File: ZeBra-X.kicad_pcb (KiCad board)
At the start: 2 copper layers, 125 parts, among them J100 CON-SOCJ-2155, Q100 T2N7002AK,LM, U100 LS1205EVD33, U101 SY8003ADFC, U102 SY8003ADFC, U103 SY8003ADFC, U104 SY8003ADFC, U105 BD3539FVM, U200 XC7Z010-2CLG400I

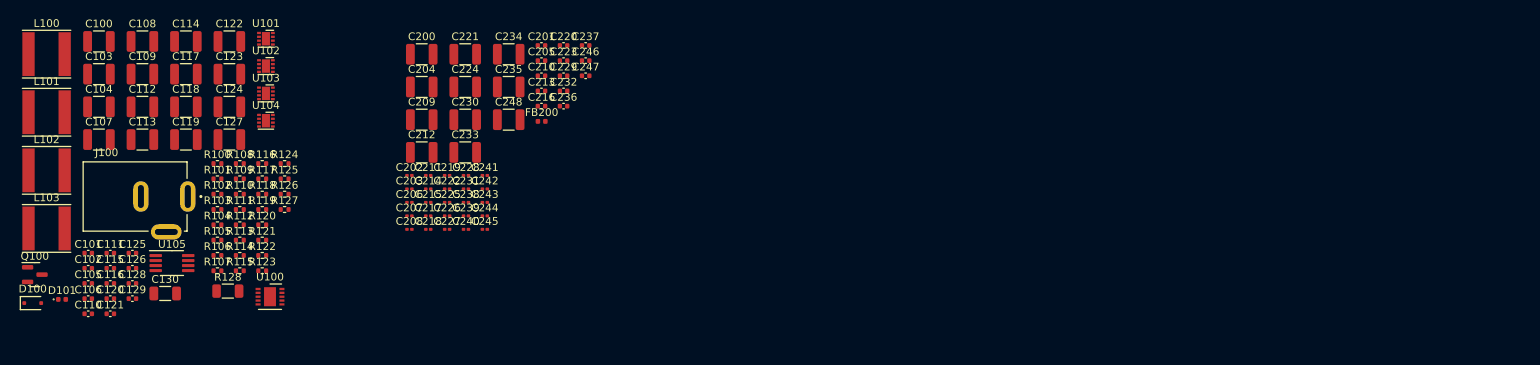
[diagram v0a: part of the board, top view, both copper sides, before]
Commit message: Finished schematic page 4: Zynq Processing System (PS), includes 128MBit QSPI flash, 33.33 MHz PS Clock, and 4Gbyte EMMC Memory
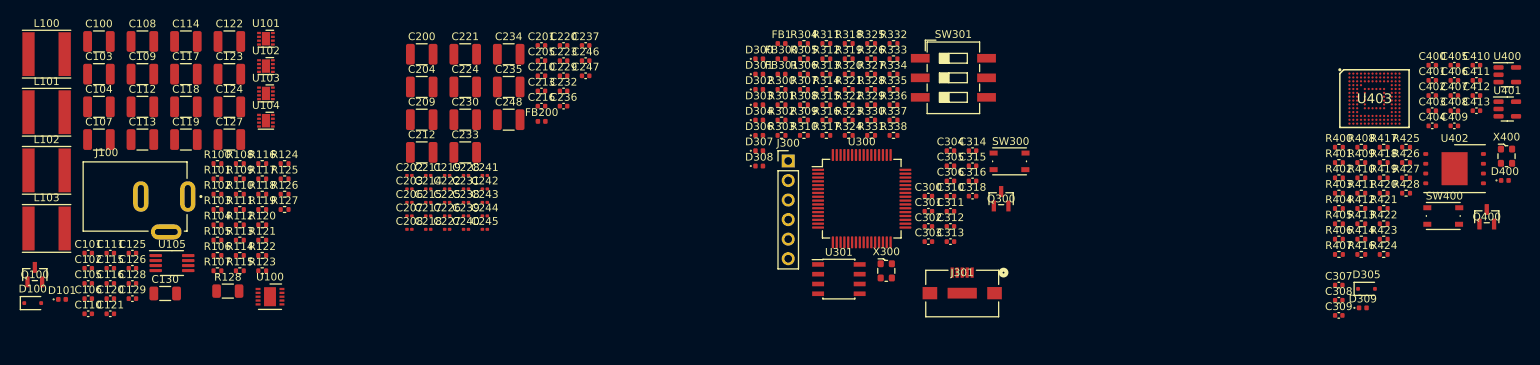
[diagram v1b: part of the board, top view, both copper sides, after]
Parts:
- added C300: 100n, Capacitor_SMD:C_0402_1005Metric, F.Cu at (135.9, 38.3)
- added C301: 4u7, Capacitor_SMD:C_0402_1005Metric, F.Cu at (135.9, 40.2)
- added C302: 4u7, Capacitor_SMD:C_0402_1005Metric, F.Cu at (135.9, 42.2)
- added C303: 4u7, Capacitor_SMD:C_0402_1005Metric, F.Cu at (135.9, 44.2)
- added C304: 100n, Capacitor_SMD:C_0402_1005Metric, F.Cu at (138.7, 32.3)
- added C305: 4u7, Capacitor_SMD:C_0402_1005Metric, F.Cu at (138.7, 34.3)
- added C306: 100n, Capacitor_SMD:C_0402_1005Metric, F.Cu at (138.7, 36.3)
- added C307: 100n, Capacitor_SMD:C_0402_1005Metric, F.Cu at (189.2, 49.8)
- added C308: 100n, Capacitor_SMD:C_0402_1005Metric, F.Cu at (189.2, 51.8)
- added C309: 100n, Capacitor_SMD:C_0402_1005Metric, F.Cu at (189.2, 53.8)
- added C310: 100n, Capacitor_SMD:C_0402_1005Metric, F.Cu at (138.7, 38.3)
- added C311: 100n, Capacitor_SMD:C_0402_1005Metric, F.Cu at (138.7, 40.2)
- added C312: 100n, Capacitor_SMD:C_0402_1005Metric, F.Cu at (138.7, 42.2)
- added C313: 100n, Capacitor_SMD:C_0402_1005Metric, F.Cu at (138.7, 44.2)
- added C314: 100n, Capacitor_SMD:C_0402_1005Metric, F.Cu at (141.6, 32.3)
- added C315: 4u7, Capacitor_SMD:C_0402_1005Metric, F.Cu at (141.6, 34.3)
- added C316: 100n, Capacitor_SMD:C_0402_1005Metric, F.Cu at (141.6, 36.3)
- added C318: 100n, Capacitor_SMD:C_0402_1005Metric, F.Cu at (141.6, 38.3)
- added C400: 100n, Capacitor_SMD:C_0402_1005Metric, F.Cu at (201.3, 21.2)
- added C401: 100n, Capacitor_SMD:C_0402_1005Metric, F.Cu at (201.3, 23.2)
- added C402: 100n, Capacitor_SMD:C_0402_1005Metric, F.Cu at (201.3, 25.2)
- added C403: 100n, Capacitor_SMD:C_0402_1005Metric, F.Cu at (201.3, 27.2)
- added C404: 100n, Capacitor_SMD:C_0402_1005Metric, F.Cu at (201.3, 29.1)
- added C405: 100n, Capacitor_SMD:C_0402_1005Metric, F.Cu at (204.2, 21.2)
- added C406: 100n, Capacitor_SMD:C_0402_1005Metric, F.Cu at (204.2, 23.2)
- added C407: 100n, Capacitor_SMD:C_0402_1005Metric, F.Cu at (204.2, 25.2)
- added C408: 4u7, Capacitor_SMD:C_0402_1005Metric, F.Cu at (204.2, 27.2)
- added C409: 100n, Capacitor_SMD:C_0402_1005Metric, F.Cu at (204.2, 29.1)
- added C410: 4u7, Capacitor_SMD:C_0402_1005Metric, F.Cu at (207.1, 21.2)
- added C411: 4u7, Capacitor_SMD:C_0402_1005Metric, F.Cu at (207.1, 23.2)
- added C412: 100n, Capacitor_SMD:C_0402_1005Metric, F.Cu at (207.1, 25.2)
- added C413: 4u7, Capacitor_SMD:C_0402_1005Metric, F.Cu at (207.1, 27.2)
- added D300: LED_GREEN, LED_SMD:LED_0402_1005Metric, F.Cu at (113.9, 20.4)
- added D301: CG0402MLU-3.3G, Diode_SMD:D_0402_1005Metric, F.Cu at (113.9, 22.4)
- added D302: CG0402MLU-3.3G, Diode_SMD:D_0402_1005Metric, F.Cu at (113.9, 24.4)
- added D303: CG0402MLU-3.3G, Diode_SMD:D_0402_1005Metric, F.Cu at (113.9, 26.4)
- added D304: CG0402MLU-3.3G, Diode_SMD:D_0402_1005Metric, F.Cu at (113.9, 28.4)
- added D305: PMEG1030EJ,115, Diode_SMD:D_SOD-323F, F.Cu at (192.8, 50.3)
- added D306: CG0402MLU-3.3G, Diode_SMD:D_0402_1005Metric, F.Cu at (113.9, 30.4)
- added D307: CG0402MLU-3.3G, Diode_SMD:D_0402_1005Metric, F.Cu at (113.9, 32.4)
- added D308: LED_GREEN, LED_SMD:LED_0402_1005Metric, F.Cu at (113.9, 34.3)
- added D309: LED_GREEN, LED_SMD:LED_0402_1005Metric, F.Cu at (192.3, 52.8)
- added D400: LED_GREEN, LED_SMD:LED_0402_1005Metric, F.Cu at (210.8, 36.2)
- added FB1: 120R, Inductor_SMD:L_0402_1005Metric, F.Cu at (116.8, 18.4)
- added FB300: 120R, Inductor_SMD:L_0402_1005Metric, F.Cu at (116.8, 20.4)
- added FB301: 120R, Inductor_SMD:L_0402_1005Metric, F.Cu at (116.8, 22.4)
- added J300: DigilentH2SHeader, Connector_PinHeader_2.54mm:PinHeader_1x06_P2.54mm_Vertical, F.Cu at (117.7, 33.7)
- added J301: USB3100-30-A, ZeBra_footprints:CONN_USB3100-30-A_GCT, F.Cu at (140.3, 50.9)
- added Q300: T2N7002AK,LM, ZeBra_footprints:SOT23_TOS, F.Cu at (145.3, 38.6)
- added Q400: T2N7002AK,LM, ZeBra_footprints:SOT23_TOS, F.Cu at (208.4, 40.9)
- added R300: 4K7, Resistor_SMD:R_0402_1005Metric, F.Cu at (116.8, 24.4)
- added R301: 4K7, Resistor_SMD:R_0402_1005Metric, F.Cu at (116.8, 26.4)
- added R302: 4K7, Resistor_SMD:R_0402_1005Metric, F.Cu at (116.8, 28.4)
- added R303: 4K7, Resistor_SMD:R_0402_1005Metric, F.Cu at (116.8, 30.4)
- added R304: 4K7, Resistor_SMD:R_0402_1005Metric, F.Cu at (119.7, 18.4)
- added R305: 22R, Resistor_SMD:R_0402_1005Metric, F.Cu at (119.7, 20.4)
- added R306: 22R, Resistor_SMD:R_0402_1005Metric, F.Cu at (119.7, 22.4)
- added R307: 22R, Resistor_SMD:R_0402_1005Metric, F.Cu at (119.7, 24.4)
- added R308: 22R, Resistor_SMD:R_0402_1005Metric, F.Cu at (119.7, 26.4)
- added R309: 510R, Resistor_SMD:R_0402_1005Metric, F.Cu at (119.7, 28.4)
- added R310: 20K, Resistor_SMD:R_0402_1005Metric, F.Cu at (119.7, 30.4)
- added R311: 1K, Resistor_SMD:R_0402_1005Metric, F.Cu at (122.6, 18.4)
- added R312: 20K, Resistor_SMD:R_0402_1005Metric, F.Cu at (122.6, 20.4)
- added R313: 1K, Resistor_SMD:R_0402_1005Metric, F.Cu at (122.6, 22.4)
- added R314: 20K, Resistor_SMD:R_0402_1005Metric, F.Cu at (122.6, 24.4)
- added R315: 1K, Resistor_SMD:R_0402_1005Metric, F.Cu at (122.6, 26.4)
- added R316: 20K, Resistor_SMD:R_0402_1005Metric, F.Cu at (122.6, 28.4)
- added R317: DNP_0R, Resistor_SMD:R_0402_1005Metric, F.Cu at (122.6, 30.4)
- added R318: 1K, Resistor_SMD:R_0402_1005Metric, F.Cu at (125.5, 18.4)
- added R319: 20K, Resistor_SMD:R_0402_1005Metric, F.Cu at (125.5, 20.4)
- added R320: DNP_0R, Resistor_SMD:R_0402_1005Metric, F.Cu at (125.5, 22.4)
- added R321: 1K, Resistor_SMD:R_0402_1005Metric, F.Cu at (125.5, 24.4)
- added R322: 100K, Resistor_SMD:R_0402_1005Metric, F.Cu at (125.5, 26.4)
- added R323: 100K, Resistor_SMD:R_0402_1005Metric, F.Cu at (125.5, 28.4)
- added R324: 12K, Resistor_SMD:R_0402_1005Metric, F.Cu at (125.5, 30.4)
- added R325: 2K49, Resistor_SMD:R_0402_1005Metric, F.Cu at (128.4, 18.4)
- added R326: 12K, Resistor_SMD:R_0402_1005Metric, F.Cu at (128.4, 20.4)
- added R327: 12K, Resistor_SMD:R_0402_1005Metric, F.Cu at (128.4, 22.4)
- added R328: 12K, Resistor_SMD:R_0402_1005Metric, F.Cu at (128.4, 24.4)
- added R329: 22R, Resistor_SMD:R_0402_1005Metric, F.Cu at (128.4, 26.4)
- added R330: 22R, Resistor_SMD:R_0402_1005Metric, F.Cu at (128.4, 28.4)
- added R331: 22R, Resistor_SMD:R_0402_1005Metric, F.Cu at (128.4, 30.4)
- added R332: 22R, Resistor_SMD:R_0402_1005Metric, F.Cu at (131.3, 18.4)
- added R333: 22R, Resistor_SMD:R_0402_1005Metric, F.Cu at (131.3, 20.4)
- added R334: 22R, Resistor_SMD:R_0402_1005Metric, F.Cu at (131.3, 22.4)
- added R335: 22R, Resistor_SMD:R_0402_1005Metric, F.Cu at (131.3, 24.4)
- added R336: 510R, Resistor_SMD:R_0402_1005Metric, F.Cu at (131.3, 26.4)
- added R337: 510R, Resistor_SMD:R_0402_1005Metric, F.Cu at (131.3, 28.4)
- added R338: 22R, Resistor_SMD:R_0402_1005Metric, F.Cu at (131.3, 30.4)
- added R400: 12K, Resistor_SMD:R_0402_1005Metric, F.Cu at (189.2, 31.9)
- added R401: 12K, Resistor_SMD:R_0402_1005Metric, F.Cu at (189.2, 33.9)
- added R402: 12K, Resistor_SMD:R_0402_1005Metric, F.Cu at (189.2, 35.9)
- added R403: 4K7, Resistor_SMD:R_0402_1005Metric, F.Cu at (189.2, 37.9)
- added R404: 20K, Resistor_SMD:R_0402_1005Metric, F.Cu at (189.2, 39.9)
- added R405: 20K, Resistor_SMD:R_0402_1005Metric, F.Cu at (189.2, 41.9)
- added R406: 22R, Resistor_SMD:R_0402_1005Metric, F.Cu at (189.2, 43.8)
- added R407: 22R, Resistor_SMD:R_0402_1005Metric, F.Cu at (189.2, 45.8)
- added R408: 22R, Resistor_SMD:R_0402_1005Metric, F.Cu at (192.1, 31.9)
- added R409: 22R, Resistor_SMD:R_0402_1005Metric, F.Cu at (192.1, 33.9)
- added R410: 22R, Resistor_SMD:R_0402_1005Metric, F.Cu at (192.1, 35.9)
- added R411: 22R, Resistor_SMD:R_0402_1005Metric, F.Cu at (192.1, 37.9)
- added R412: 510R, Resistor_SMD:R_0402_1005Metric, F.Cu at (192.1, 39.9)
- added R413: 12K, Resistor_SMD:R_0402_1005Metric, F.Cu at (192.1, 41.9)
- added R414: 100K, Resistor_SMD:R_0402_1005Metric, F.Cu at (192.1, 43.8)
- added R416: 100K, Resistor_SMD:R_0402_1005Metric, F.Cu at (192.1, 45.8)
- added R417: 12K, Resistor_SMD:R_0402_1005Metric, F.Cu at (195.0, 31.9)
- added R418: 12K, Resistor_SMD:R_0402_1005Metric, F.Cu at (195.0, 33.9)
- added R419: 22R, Resistor_SMD:R_0402_1005Metric, F.Cu at (195.0, 35.9)
- added R420: 22R, Resistor_SMD:R_0402_1005Metric, F.Cu at (195.0, 37.9)
- added R421: 68K, Resistor_SMD:R_0402_1005Metric, F.Cu at (195.0, 39.9)
- added R422: 68K, Resistor_SMD:R_0402_1005Metric, F.Cu at (195.0, 41.9)
- added R423: 68K, Resistor_SMD:R_0402_1005Metric, F.Cu at (195.0, 43.8)
- added R424: 68K, Resistor_SMD:R_0402_1005Metric, F.Cu at (195.0, 45.8)
- added R425: 12K, Resistor_SMD:R_0402_1005Metric, F.Cu at (197.9, 31.9)
- added R426: 12K, Resistor_SMD:R_0402_1005Metric, F.Cu at (197.9, 33.9)
- added R427: 22R, Resistor_SMD:R_0402_1005Metric, F.Cu at (197.9, 35.9)
- added R428: DNP_0R, Resistor_SMD:R_0402_1005Metric, F.Cu at (197.9, 37.9)
- added SW300: SKRPANE010, Button_Switch_SMD:SW_Push_1P1T_NO_Vertical_Wuerth_434133025816, F.Cu at (146.4, 33.7)
- added SW301: 219-3LPST, Button_Switch_SMD:SW_DIP_SPSTx03_Slide_6.7x9.18mm_W8.61mm_P2.54mm_LowProfile, F.Cu at (139.1, 22.9)
- added SW400: SKRPANE010, Button_Switch_SMD:SW_Push_1P1T_NO_Vertical_Wuerth_434133025816, F.Cu at (202.8, 40.8)
- added U300: FT2232HL, Package_QFP:LQFP-64_10x10mm_P0.5mm, F.Cu at (127.2, 38.6)
- added U301: 93LC65B-I/SN, ZeBra_footprints:SOIC-8_3.9x4.9mm_P1.27mm, F.Cu at (124.2, 49.0)
- added U400: 74LVC1G07, Package_TO_SOT_SMD:SOT-23-5, F.Cu at (211.1, 22.5)
- added U401: 74LVC1G07, Package_TO_SOT_SMD:SOT-23-5, F.Cu at (211.1, 26.9)
- added U402: W25Q128JVEIQ, Package_SON:WSON-8-1EP_8x6mm_P1.27mm_EP3.4x4.3mm, F.Cu at (204.2, 34.7)
- added U403: S40FC004C1B2C00000, ZeBra_footprints:BGA153C50P14X14_900X750X80, F.Cu at (193.8, 25.6)
- added X300: ECS-2520MV-120-BN, Oscillator:Oscillator_SMD_ECS_2520MV-xxx-xx-4Pin_2.5x2.0mm, F.Cu at (130.4, 48.0)
- added X400: ECS-2520MV-333.3-BN-TR, Oscillator:Oscillator_SMD_ECS_2520MV-xxx-xx-4Pin_2.5x2.0mm, F.Cu at (211.0, 33.1)
- Q100: footprint Package_TO_SOT_SMD:SOT-23 -> ZeBra_footprints:SOT23_TOS
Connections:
- Q100 pad 1: /[1] Power/LED_PWR_K -> Net-(Q100-G)
- Q100 pad 2: Net-(Q100-G) -> GND
- Q100 pad 3: GND -> /[1] Power/LED_PWR_K
- U200 pad A10: (no net) -> USB_DATA5
- U200 pad A11: (no net) -> USB_CLK
- U200 pad A12: (no net) -> USB_DATA2
- U200 pad A14: (no net) -> USB_DATA0
- U200 pad A15: (no net) -> ETH_RXD3
- U200 pad A16: (no net) -> ETH_RXD1
- U200 pad A17: (no net) -> /[4] Zynq Processing System (PS)/ETH_TXD3
- U200 pad A19: (no net) -> /[4] Zynq Processing System (PS)/ETH_TXCLK
- U200 pad A5: (no net) -> /[4] Zynq Processing System (PS)/QSPI_CLK
- U200 pad A6: (no net) -> QSPI_DQ3_M0
- U200 pad A7: (no net) -> /[4] Zynq Processing System (PS)/QSPI_NCS
- U200 pad A9: (no net) -> MIO43
- U200 pad B10: (no net) -> /[4] Zynq Processing System (PS)/PS_NRST
- U200 pad B12: (no net) -> MIO48
- U200 pad B13: (no net) -> MIO50
- U200 pad B14: (no net) -> MIO47
- U200 pad B15: (no net) -> MIO45
- U200 pad B17: (no net) -> ETH_RXCLK
- U200 pad B18: (no net) -> /[4] Zynq Processing System (PS)/ETH_TXD1
- U200 pad B5: (no net) -> UART1_RX
- U200 pad B7: (no net) -> QSPI_DQ2_M2
- U200 pad B8: (no net) -> QSPI_DQ0_M3
- U200 pad B9: (no net) -> MIO51
- U200 pad C10: (no net) -> ETH_MDC
- U200 pad C11: (no net) -> ETH_MDIO
- U200 pad C12: (no net) -> MIO49
- U200 pad C13: (no net) -> USB_DIR
- U200 pad C15: (no net) -> USB_STP
- U200 pad C16: (no net) -> USB_DATA4
- U200 pad C17: (no net) -> /[4] Zynq Processing System (PS)/ETH_NRST
- U200 pad C18: (no net) -> USB_DATA7
- U200 pad C5: (no net) -> /[4] Zynq Processing System (PS)/SD_D2
- U200 pad C6: (no net) -> /[4] Zynq Processing System (PS)/SD_CMD
- U200 pad C7: (no net) -> PS_NPOR
- U200 pad C8: (no net) -> /[4] Zynq Processing System (PS)/SD_D3
- U200 pad D10: (no net) -> /[4] Zynq Processing System (PS)/ETH_TXD2
- U200 pad D11: (no net) -> ETH_RXD0
- U200 pad D13: (no net) -> ETH_RXCTL
- U200 pad D14: (no net) -> USB_NRST
- U200 pad D15: (no net) -> USB_DATA1
- U200 pad D16: (no net) -> MIO46
- U200 pad D5: (no net) -> UART1_TX_VCFG1
- U200 pad D6: (no net) -> QSPI_DQ1_M1
- U200 pad D8: (no net) -> /[4] Zynq Processing System (PS)/VCFG0
- U200 pad D9: (no net) -> /[4] Zynq Processing System (PS)/SD_CLK
- U200 pad E11: (no net) -> /[4] Zynq Processing System (PS)/MIO_VREF_0V9
- U200 pad E12: (no net) -> ETH_NINT
- U200 pad E13: (no net) -> USB_DATA6
- U200 pad E14: (no net) -> /[4] Zynq Processing System (PS)/ETH_TXD0
- U200 pad E16: (no net) -> USB_NXT
- U200 pad E6: (no net) -> /[4] Zynq Processing System (PS)/PS_LED
- U200 pad E7: (no net) -> /[4] Zynq Processing System (PS)/PS_CLK_33M333
- U200 pad E8: (no net) -> /[4] Zynq Processing System (PS)/SD_D1
- U200 pad E9: (no net) -> /[4] Zynq Processing System (PS)/SD_D0
- U200 pad F12: (no net) -> USB_DATA3
- U200 pad F13: (no net) -> MIO44
- U200 pad F14: (no net) -> /[4] Zynq Processing System (PS)/ETH_TXCTL
- U200 pad F15: (no net) -> ETH_RXD2
- U200 pad F6: (no net) -> /[3] Config, JTAG, Debug/TDO
- U200 pad F9: (no net) -> /[3] Config, JTAG, Debug/TCK
- U200 pad G6: (no net) -> /[3] Config, JTAG, Debug/TDI
- U200 pad J6: (no net) -> /[3] Config, JTAG, Debug/TMS
- U200 pad K10: (no net) -> GND
- U200 pad K9: (no net) -> GND
- U200 pad L10: (no net) -> GND
- U200 pad L6: (no net) -> /[3] Config, JTAG, Debug/NPROGRAM
- U200 pad L9: (no net) -> GND
- U200 pad M10: (no net) -> GND
- U200 pad M6: (no net) -> +3V3
- U200 pad M9: (no net) -> GND
- U200 pad R10: (no net) -> /[3] Config, JTAG, Debug/NINIT
- U200 pad R11: (no net) -> /[3] Config, JTAG, Debug/DONE

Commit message: Added page '[7] 1GB DDR3L Modules'
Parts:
- added C600: 47n, Capacitor_SMD:C_0201_0603Metric, F.Cu at (225.9, 34.7)
- added C601: 47n, Capacitor_SMD:C_0201_0603Metric, F.Cu at (225.9, 36.4)
- added C602: 47n, Capacitor_SMD:C_0201_0603Metric, F.Cu at (225.9, 38.2)
- added C603: 47n, Capacitor_SMD:C_0201_0603Metric, F.Cu at (225.9, 39.9)
- added C604: 470n, Capacitor_SMD:C_0201_0603Metric, F.Cu at (225.9, 41.7)
- added C605: 470n, Capacitor_SMD:C_0201_0603Metric, F.Cu at (225.9, 43.4)
- added C606: 470n, Capacitor_SMD:C_0201_0603Metric, F.Cu at (225.9, 45.2)
- added C607: 470n, Capacitor_SMD:C_0201_0603Metric, F.Cu at (225.9, 46.9)
- added C608: 4u7, Capacitor_SMD:C_0402_1005Metric, F.Cu at (238.4, 34.8)
- added C609: 4u7, Capacitor_SMD:C_0402_1005Metric, F.Cu at (238.4, 36.8)
- added C610: 4u7, Capacitor_SMD:C_0402_1005Metric, F.Cu at (238.4, 38.7)
- added C611: 4u7, Capacitor_SMD:C_0402_1005Metric, F.Cu at (238.4, 40.7)
- added C612: 47n, Capacitor_SMD:C_0201_0603Metric, F.Cu at (228.4, 34.7)
- added C613: 47n, Capacitor_SMD:C_0201_0603Metric, F.Cu at (228.4, 36.4)
- added C700: 47n, Capacitor_SMD:C_0201_0603Metric, F.Cu at (214.0, 57.1)
- added C701: 47n, Capacitor_SMD:C_0201_0603Metric, F.Cu at (214.0, 58.8)
- added C702: 4u7, Capacitor_SMD:C_0402_1005Metric, F.Cu at (224.1, 57.2)
- added C703: 470n, Capacitor_SMD:C_0201_0603Metric, F.Cu at (214.0, 60.6)
- added C704: 47n, Capacitor_SMD:C_0201_0603Metric, F.Cu at (214.0, 62.3)
- added C705: 47n, Capacitor_SMD:C_0201_0603Metric, F.Cu at (214.0, 64.1)
- added C706: 47n, Capacitor_SMD:C_0201_0603Metric, F.Cu at (216.5, 57.1)
- added C707: 47n, Capacitor_SMD:C_0201_0603Metric, F.Cu at (216.5, 58.8)
- added C708: 47n, Capacitor_SMD:C_0201_0603Metric, F.Cu at (216.5, 60.6)
- added C709: 47n, Capacitor_SMD:C_0201_0603Metric, F.Cu at (216.5, 62.3)
- added C710: 47n, Capacitor_SMD:C_0201_0603Metric, F.Cu at (216.5, 64.1)
- added C711: 47n, Capacitor_SMD:C_0201_0603Metric, F.Cu at (218.9, 57.1)
- added C712: 4u7, Capacitor_SMD:C_0402_1005Metric, F.Cu at (224.1, 59.2)
- added C713: 470n, Capacitor_SMD:C_0201_0603Metric, F.Cu at (218.9, 58.8)
- added C714: 47n, Capacitor_SMD:C_0201_0603Metric, F.Cu at (218.9, 60.6)
- added C715: 47n, Capacitor_SMD:C_0201_0603Metric, F.Cu at (218.9, 62.3)
- added C716: 47n, Capacitor_SMD:C_0201_0603Metric, F.Cu at (218.9, 64.1)
- added C717: 47n, Capacitor_SMD:C_0201_0603Metric, F.Cu at (221.4, 57.1)
- added C718: 47n, Capacitor_SMD:C_0201_0603Metric, F.Cu at (221.4, 58.8)
- added C719: 47n, Capacitor_SMD:C_0201_0603Metric, F.Cu at (221.4, 60.6)
- added C720: 47n, Capacitor_SMD:C_0201_0603Metric, F.Cu at (221.4, 62.3)
- added C721: 47n, Capacitor_SMD:C_0201_0603Metric, F.Cu at (221.4, 64.1)
- added C722: 47n, Capacitor_SMD:C_0201_0603Metric, F.Cu at (213.0, 75.2)
- added C723: 47n, Capacitor_SMD:C_0201_0603Metric, F.Cu at (213.0, 77.0)
- added C724: 4u7, Capacitor_SMD:C_0402_1005Metric, F.Cu at (223.0, 75.3)
- added C725: 470n, Capacitor_SMD:C_0201_0603Metric, F.Cu at (213.0, 78.7)
- added C726: 47n, Capacitor_SMD:C_0201_0603Metric, F.Cu at (213.0, 80.5)
- added C727: 47n, Capacitor_SMD:C_0201_0603Metric, F.Cu at (213.0, 82.2)
- added C728: 47n, Capacitor_SMD:C_0201_0603Metric, F.Cu at (215.4, 75.2)
- added C729: 47n, Capacitor_SMD:C_0201_0603Metric, F.Cu at (215.4, 77.0)
- added C730: 47n, Capacitor_SMD:C_0201_0603Metric, F.Cu at (215.4, 78.7)
- added C731: 47n, Capacitor_SMD:C_0201_0603Metric, F.Cu at (215.4, 80.5)
- added C732: 47n, Capacitor_SMD:C_0201_0603Metric, F.Cu at (215.4, 82.2)
- added C733: 47n, Capacitor_SMD:C_0201_0603Metric, F.Cu at (217.9, 75.2)
- added C734: 4u7, Capacitor_SMD:C_0402_1005Metric, F.Cu at (223.0, 77.3)
- added C735: 470n, Capacitor_SMD:C_0201_0603Metric, F.Cu at (217.9, 77.0)
- added C736: 47n, Capacitor_SMD:C_0201_0603Metric, F.Cu at (217.9, 78.7)
- added C737: 47n, Capacitor_SMD:C_0201_0603Metric, F.Cu at (217.9, 80.5)
- added C738: 47n, Capacitor_SMD:C_0201_0603Metric, F.Cu at (217.9, 82.2)
- added C739: 47n, Capacitor_SMD:C_0201_0603Metric, F.Cu at (220.3, 75.2)
- added C740: 47n, Capacitor_SMD:C_0201_0603Metric, F.Cu at (220.3, 77.0)
- added C741: 47n, Capacitor_SMD:C_0201_0603Metric, F.Cu at (220.3, 78.7)
- added C742: 47n, Capacitor_SMD:C_0201_0603Metric, F.Cu at (220.3, 80.5)
- added C743: 47n, Capacitor_SMD:C_0201_0603Metric, F.Cu at (220.3, 82.2)
- added D500: LED_GREEN, LED_SMD:LED_0402_1005Metric, F.Cu at (253.4, 44.8)
- added Q500: T2N7002AK,LM, ZeBra_footprints:SOT23_TOS, F.Cu at (253.9, 41.4)
- added R500: 1K, Resistor_SMD:R_0402_1005Metric, F.Cu at (250.2, 39.9)
- added R501: 100K, Resistor_SMD:R_0402_1005Metric, F.Cu at (250.2, 41.9)
- added R502: 12K, Resistor_SMD:R_0402_1005Metric, F.Cu at (250.2, 43.9)
- added R503: 510R, Resistor_SMD:R_0402_1005Metric, F.Cu at (250.2, 45.8)
- added R600: 100R, Resistor_SMD:R_0201_0603Metric, F.Cu at (228.4, 38.2)
- added R601: 49R9, Resistor_SMD:R_0201_0603Metric, F.Cu at (228.4, 39.9)
- added R602: 49R9, Resistor_SMD:R_0201_0603Metric, F.Cu at (228.4, 41.7)
- added R603: 49R9, Resistor_SMD:R_0201_0603Metric, F.Cu at (228.4, 43.4)
- added R604: 49R9, Resistor_SMD:R_0201_0603Metric, F.Cu at (228.4, 45.2)
- added R605: 49R9, Resistor_SMD:R_0201_0603Metric, F.Cu at (228.4, 46.9)
- added R606: 49R9, Resistor_SMD:R_0201_0603Metric, F.Cu at (230.8, 34.7)
- added R607: 49R9, Resistor_SMD:R_0201_0603Metric, F.Cu at (230.8, 36.4)
- added R608: 49R9, Resistor_SMD:R_0201_0603Metric, F.Cu at (230.8, 38.2)
- added R609: 49R9, Resistor_SMD:R_0201_0603Metric, F.Cu at (230.8, 39.9)
- added R610: 49R9, Resistor_SMD:R_0201_0603Metric, F.Cu at (230.8, 41.7)
- added R611: 49R9, Resistor_SMD:R_0201_0603Metric, F.Cu at (230.8, 43.4)
- added R612: 49R9, Resistor_SMD:R_0201_0603Metric, F.Cu at (230.8, 45.2)
- added R613: 49R9, Resistor_SMD:R_0201_0603Metric, F.Cu at (230.8, 46.9)
- added R614: 49R9, Resistor_SMD:R_0201_0603Metric, F.Cu at (233.3, 34.7)
- added R615: 49R9, Resistor_SMD:R_0201_0603Metric, F.Cu at (233.3, 36.4)
- added R616: 49R9, Resistor_SMD:R_0201_0603Metric, F.Cu at (233.3, 38.2)
- added R617: 49R9, Resistor_SMD:R_0201_0603Metric, F.Cu at (233.3, 39.9)
- added R618: 49R9, Resistor_SMD:R_0201_0603Metric, F.Cu at (233.3, 41.7)
- added R619: 49R9, Resistor_SMD:R_0201_0603Metric, F.Cu at (233.3, 43.4)
- added R620: 49R9, Resistor_SMD:R_0201_0603Metric, F.Cu at (233.3, 45.2)
- added R621: 49R9, Resistor_SMD:R_0201_0603Metric, F.Cu at (233.3, 46.9)
- added R622: 49R9, Resistor_SMD:R_0201_0603Metric, F.Cu at (235.7, 34.7)
- added R623: 49R9, Resistor_SMD:R_0201_0603Metric, F.Cu at (235.7, 36.4)
- added R624: 49R9, Resistor_SMD:R_0201_0603Metric, F.Cu at (235.7, 38.2)
- added R625: 4K7, Resistor_SMD:R_0402_1005Metric, F.Cu at (238.4, 42.7)
- added R626: 100R, Resistor_SMD:R_0201_0603Metric, F.Cu at (235.7, 39.9)
- added R627: 100R, Resistor_SMD:R_0201_0603Metric, F.Cu at (235.7, 41.7)
- added R700: 240R, Resistor_SMD:R_0402_1005Metric, F.Cu at (248.3, 61.4)
- added R701: 240R, Resistor_SMD:R_0402_1005Metric, F.Cu at (248.3, 63.4)
- added U700: MT41K256M16TW-107 IT:P, ZeBra_footprints:FBGA96_TW_MRN, F.Cu at (234.3, 60.8)
- added U701: MT41K256M16TW-107 IT:P, ZeBra_footprints:FBGA96_TW_MRN, F.Cu at (234.3, 79.0)
- moved U200 26.4 mm to (44.0, 97.1)
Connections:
- U200 pad A1: (no net) -> DDR_DM0
- U200 pad A2: (no net) -> DDR_DQ2
- U200 pad A20: (no net) -> unconnected-(U200B-IO_L2N_T0_AD8N_35-PadA20)
- U200 pad A4: (no net) -> DDR_DQ3
- U200 pad B19: (no net) -> unconnected-(U200B-IO_L2P_T0_AD8P_35-PadB19)
- U200 pad B2: (no net) -> DDR_DQS0_N
- U200 pad B20: (no net) -> unconnected-(U200B-IO_L1N_T0_AD0N_35-PadB20)
- U200 pad B3: (no net) -> DDR_DQ1
- U200 pad B4: (no net) -> DDR_NRST
- U200 pad C1: (no net) -> DDR_DQ6
- U200 pad C2: (no net) -> DDR_DQS0_P
- U200 pad C20: (no net) -> unconnected-(U200B-IO_L1P_T0_AD0P_35-PadC20)
- U200 pad C3: (no net) -> DDR_DQ0
- U200 pad D1: (no net) -> DDR_DQ5
- U200 pad D18: (no net) -> PL_B35_L3_N
- U200 pad D19: (no net) -> unconnected-(U200B-IO_L4P_T0_35-PadD19)
- U200 pad D20: (no net) -> unconnected-(U200B-IO_L4N_T0_35-PadD20)
- U200 pad D3: (no net) -> DDR_DQ4
- U200 pad D4: (no net) -> DDR_A13
- U200 pad E1: (no net) -> DDR_DQ7
- U200 pad E17: (no net) -> PL_B35_L3_P
- U200 pad E18: (no net) -> PL_B35_L5_P
- U200 pad E19: (no net) -> PL_B35_L5_N
- U200 pad E2: (no net) -> DDR_DQ8
- U200 pad E3: (no net) -> DDR_DQ9
- U200 pad E4: (no net) -> DDR_A12
- U200 pad F1: (no net) -> DDR_DM1
- U200 pad F16: (no net) -> PL_B35_L6_P
- U200 pad F17: (no net) -> PL_B35_L6_N
- U200 pad F19: (no net) -> unconnected-(U200B-IO_L15P_T2_DQS_AD12P_35-PadF19)
- U200 pad F2: (no net) -> DDR_DQS1_N
- U200 pad F20: (no net) -> unconnected-(U200B-IO_L15N_T2_DQS_AD12N_35-PadF20)
- U200 pad F4: (no net) -> DDR_A14
- U200 pad F5: (no net) -> DDR_A10
- U200 pad G14: (no net) -> unconnected-(U200B-IO_0_35-PadG14)
- U200 pad G15: (no net) -> unconnected-(U200B-IO_L19N_T3_VREF_35-PadG15)
- U200 pad G17: (no net) -> PL_B35_L16_P
- U200 pad G18: (no net) -> PL_B35_L16_N
- U200 pad G19: (no net) -> unconnected-(U200B-IO_L18P_T2_AD13P_35-PadG19)
- U200 pad G2: (no net) -> DDR_DQS1_P
- U200 pad G20: (no net) -> unconnected-(U200B-IO_L18N_T2_AD13N_35-PadG20)
- U200 pad G3: (no net) -> DDR_DQ10
- U200 pad G4: (no net) -> DDR_A11
- U200 pad G5: (no net) -> /[6] Zynq DDR Interface & Termination/DDR_VRN
- U200 pad H1: (no net) -> DDR_DQ14
- U200 pad H15: (no net) -> unconnected-(U200B-IO_L19P_T3_35-PadH15)
- U200 pad H16: (no net) -> PL_B35_L13_P
- U200 pad H17: (no net) -> PL_B35_L13_N
- U200 pad H18: (no net) -> PL_B35_L14_N
- U200 pad H2: (no net) -> DDR_DQ13
- U200 pad H20: (no net) -> unconnected-(U200B-IO_L17N_T2_AD5N_35-PadH20)
- U200 pad H3: (no net) -> DDR_DQ11
- U200 pad H5: (no net) -> /[6] Zynq DDR Interface & Termination/DDR_VRP
- U200 pad H6: (no net) -> +0V675_REF
- U200 pad J1: (no net) -> DDR_DQ15
- U200 pad J14: (no net) -> PL_B35_L20_N
- U200 pad J15: (no net) -> PL_B35_IO25
- U200 pad J16: (no net) -> PL_B35_L24_P
- U200 pad J18: (no net) -> PL_B35_L14_P
- U200 pad J19: (no net) -> unconnected-(U200B-IO_L10N_T1_AD11N_35-PadJ19)
- U200 pad J20: (no net) -> unconnected-(U200B-IO_L17P_T2_AD5P_35-PadJ20)
- U200 pad J3: (no net) -> DDR_DQ12
- U200 pad J4: (no net) -> DDR_A9
- U200 pad J5: (no net) -> DDR_BA2
- U200 pad K1: (no net) -> DDR_A8
- U200 pad K14: (no net) -> PL_B35_L20_P
- U200 pad K16: (no net) -> unconnected-(U200B-IO_L24P_T3_AD15P_35-PadK16)
- U200 pad K17: (no net) -> PL_CLK_125MHZ
- U200 pad K18: (no net) -> unconnected-(U200B-IO_L12N_T1_MRCC_35-PadK18)
- U200 pad K19: (no net) -> unconnected-(U200B-IO_L10P_T1_AD11P_35-PadK19)
- U200 pad K2: (no net) -> DDR_A1
- U200 pad K3: (no net) -> DDR_A3
- U200 pad K4: (no net) -> DDR_A7
- U200 pad L1: (no net) -> DDR_A5
- U200 pad L14: (no net) -> PL_B35_L22_P
- U200 pad L15: (no net) -> PL_B35_L22_N
- U200 pad L16: (no net) -> unconnected-(U200B-IO_L11P_T1_SRCC_35-PadL16)
- U200 pad L17: (no net) -> PL_B35_L11_N
- U200 pad L19: (no net) -> PL_B35_L9_P
- U200 pad L2: (no net) -> DDR_CK_P
- U200 pad L20: (no net) -> PL_B35_L9_N
- U200 pad L4: (no net) -> DDR_A6
- U200 pad L5: (no net) -> DDR_BA0
- U200 pad M14: (no net) -> PL_B35_L23_P
- U200 pad M15: (no net) -> PL_B35_L23_N
- U200 pad M17: (no net) -> PL_B35_L8_P
- U200 pad M18: (no net) -> PL_B35_L8_N
- U200 pad M19: (no net) -> PL_B35_L7_P
- U200 pad M2: (no net) -> DDR_CK_N
- U200 pad M20: (no net) -> PL_B35_L7_N
- U200 pad M3: (no net) -> DDR_A2
- U200 pad M4: (no net) -> DDR_A4
- U200 pad M5: (no net) -> DDR_NWE
- U200 pad N1: (no net) -> DDR_NCS
- U200 pad N15: (no net) -> unconnected-(U200B-IO_L21P_T3_DQS_AD14P_35-PadN15)
- U200 pad N16: (no net) -> unconnected-(U200B-IO_L21N_T3_DQS_AD14N_35-PadN16)
- U200 pad N17: (no net) -> unconnected-(U200A-IO_L23P_T3_34-PadN17)
- U200 pad N18: (no net) -> unconnected-(U200A-IO_L13P_T2_MRCC_34-PadN18)
- U200 pad N2: (no net) -> DDR_A0
- U200 pad N20: (no net) -> PL_B34_L14_P
- U200 pad N3: (no net) -> DDR_CKE
- U200 pad N5: (no net) -> DDR_ODT
- U200 pad P1: (no net) -> DDR_DQ16
- U200 pad P14: (no net) -> unconnected-(U200A-IO_L6P_T0_34-PadP14)
- U200 pad P15: (no net) -> unconnected-(U200A-IO_L24P_T3_34-PadP15)
- U200 pad P16: (no net) -> unconnected-(U200A-IO_L24N_T3_34-PadP16)
- U200 pad P18: (no net) -> unconnected-(U200A-IO_L23N_T3_34-PadP18)
- U200 pad P19: (no net) -> unconnected-(U200A-IO_L13N_T2_MRCC_34-PadP19)
- U200 pad P20: (no net) -> PL_B34_L14_N
- U200 pad P3: (no net) -> DDR_DQ17
- U200 pad P4: (no net) -> DDR_NRAS
- U200 pad P5: (no net) -> DDR_NCAS
- U200 pad P6: (no net) -> +0V675_REF
- U200 pad R1: (no net) -> DDR_DQ19
- U200 pad R14: (no net) -> unconnected-(U200A-IO_L6N_T0_VREF_34-PadR14)
- U200 pad R16: (no net) -> unconnected-(U200A-IO_L19P_T3_34-PadR16)
- U200 pad R17: (no net) -> unconnected-(U200A-IO_L19N_T3_VREF_34-PadR17)
- U200 pad R19: (no net) -> unconnected-(U200A-IO_0_34-PadR19)
- U200 pad R2: (no net) -> DDR_DQS2_P
- U200 pad R3: (no net) -> DDR_DQ18
- U200 pad R4: (no net) -> DDR_BA1
- U200 pad T1: (no net) -> DDR_DM2
- U200 pad T10: (no net) -> unconnected-(U200A-IO_L1N_T0_34-PadT10)
- U200 pad T11: (no net) -> unconnected-(U200A-IO_L1P_T0_34-PadT11)
- U200 pad T12: (no net) -> /[5] Zynq Programmable Logic (PL)/LED_PL
- U200 pad T14: (no net) -> unconnected-(U200A-IO_L5P_T0_34-PadT14)
- U200 pad T15: (no net) -> unconnected-(U200A-IO_L5N_T0_34-PadT15)
- U200 pad T16: (no net) -> unconnected-(U200A-IO_L9P_T1_DQS_34-PadT16)
- U200 pad T17: (no net) -> unconnected-(U200A-IO_L20P_T3_34-PadT17)
- U200 pad T19: (no net) -> unconnected-(U200A-IO_25_34-PadT19)
- U200 pad T2: (no net) -> DDR_DQS2_N
- U200 pad T20: (no net) -> PL_B34_L15_P
- U200 pad T4: (no net) -> DDR_DQ20
- U200 pad U12: (no net) -> unconnected-(U200A-IO_L2N_T0_34-PadU12)
- U200 pad U13: (no net) -> /[5] Zynq Programmable Logic (PL)/NPUDC
- U200 pad U14: (no net) -> PL_B34_L11_P
- U200 pad U15: (no net) -> PL_B34_L11_N
- U200 pad U17: (no net) -> unconnected-(U200A-IO_L9N_T1_DQS_34-PadU17)
- U200 pad U18: (no net) -> unconnected-(U200A-IO_L12P_T1_MRCC_34-PadU18)
- U200 pad U19: (no net) -> unconnected-(U200A-IO_L12N_T1_MRCC_34-PadU19)
- U200 pad U2: (no net) -> DDR_DQ22
- U200 pad U20: (no net) -> PL_B34_L15_N
- U200 pad U3: (no net) -> DDR_DQ23
- U200 pad U4: (no net) -> DDR_DQ21
- U200 pad V1: (no net) -> DDR_DQ24
- U200 pad V12: (no net) -> PL_B34_L4_P
- U200 pad V13: (no net) -> unconnected-(U200A-IO_L3N_T0_DQS_34-PadV13)
- U200 pad V15: (no net) -> PL_B34_L10_P
- U200 pad V16: (no net) -> PL_B34_L18_P
- U200 pad V17: (no net) -> unconnected-(U200A-IO_L21P_T3_DQS_34-PadV17)
- U200 pad V18: (no net) -> unconnected-(U200A-IO_L21N_T3_DQS_34-PadV18)
- U200 pad V2: (no net) -> DDR_DQ30
- U200 pad V20: (no net) -> PL_B34_L16_P
- U200 pad V3: (no net) -> DDR_DQ31
- U200 pad W1: (no net) -> DDR_DQ26
- U200 pad W13: (no net) -> PL_B34_L4_N
- U200 pad W14: (no net) -> PL_B34_L8_P
- U200 pad W15: (no net) -> PL_B34_L10_N
- U200 pad W16: (no net) -> PL_B34_L18_N
- U200 pad W18: (no net) -> PL_B34_L22_P
- U200 pad W19: (no net) -> PL_B34_L22_N
- U200 pad W20: (no net) -> PL_B34_L16_N
- U200 pad W3: (no net) -> DDR_DQ29
- U200 pad W4: (no net) -> DDR_DQS3_N
- U200 pad W5: (no net) -> DDR_DQS3_P
- U200 pad Y1: (no net) -> DDR_DM3
- U200 pad Y14: (no net) -> PL_B34_L8_N
- U200 pad Y16: (no net) -> PL_B34_L7_P
- U200 pad Y17: (no net) -> PL_B34_L7_N
- U200 pad Y18: (no net) -> PL_B34_L17_P
- U200 pad Y19: (no net) -> PL_B34_L17_N
- U200 pad Y2: (no net) -> DDR_DQ28
- U200 pad Y3: (no net) -> DDR_DQ25
- U200 pad Y4: (no net) -> DDR_DQ27
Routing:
- added copper zone on F.Cu, net GND
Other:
- board outline added: 255.3 x 107.1 mm

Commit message: Completed page 8, Gigabit Ethernet Controller
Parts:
- added C800: 4u7, Capacitor_SMD:C_0402_1005Metric, F.Cu at (155.3, 83.5)
- added C801: 100n, Capacitor_SMD:C_0402_1005Metric, F.Cu at (155.3, 85.5)
- added C802: 100n, Capacitor_SMD:C_0402_1005Metric, F.Cu at (155.3, 87.4)
- added C803: 100n, Capacitor_SMD:C_0402_1005Metric, F.Cu at (155.3, 89.4)
- added C804: 100n, Capacitor_SMD:C_0402_1005Metric, F.Cu at (155.3, 91.4)
- added C805: 100n, Capacitor_SMD:C_0402_1005Metric, F.Cu at (158.1, 83.5)
- added C806: 100n, Capacitor_SMD:C_0402_1005Metric, F.Cu at (158.1, 85.5)
- added C807: 100n, Capacitor_SMD:C_0402_1005Metric, F.Cu at (158.1, 87.4)
- added C808: 100n, Capacitor_SMD:C_0402_1005Metric, F.Cu at (158.1, 89.4)
- added C809: 4u7, Capacitor_SMD:C_0402_1005Metric, F.Cu at (158.1, 91.4)
- added C810: 100n, Capacitor_SMD:C_0402_1005Metric, F.Cu at (161.0, 83.5)
- added C811: 100n, Capacitor_SMD:C_0402_1005Metric, F.Cu at (161.0, 85.5)
- added C812: 4u7, Capacitor_SMD:C_0402_1005Metric, F.Cu at (161.0, 87.4)
- added C813: 100n, Capacitor_SMD:C_0402_1005Metric, F.Cu at (161.0, 89.4)
- added C814: 100n, Capacitor_SMD:C_0402_1005Metric, F.Cu at (161.0, 91.4)
- added C815: 4u7, Capacitor_SMD:C_0402_1005Metric, F.Cu at (163.9, 83.5)
- added C816: 4u7, Capacitor_SMD:C_0402_1005Metric, F.Cu at (163.9, 85.5)
- added C817: 100n, Capacitor_SMD:C_0402_1005Metric, F.Cu at (163.9, 87.4)
- added C818: 100n, Capacitor_SMD:C_0402_1005Metric, F.Cu at (163.9, 89.4)
- added C819: 4u7, Capacitor_SMD:C_0402_1005Metric, F.Cu at (163.9, 91.4)
- added FB302: 120R, Inductor_SMD:L_0402_1005Metric, F.Cu at (135.7, 101.7)
- added FB800: 120R, Inductor_SMD:L_0402_1005Metric, F.Cu at (155.3, 69.6)
- added J800: HR911130A, ZeBra_footprints:HANRUN_HR911130A, F.Cu at (144.0, 80.3)
- added L800: 3u3, Inductor_SMD:L_0603_1608Metric, F.Cu at (147.4, 92.7)
- added R800: 4K7, Resistor_SMD:R_0402_1005Metric, F.Cu at (155.3, 71.6)
- added R801: 4K7, Resistor_SMD:R_0402_1005Metric, F.Cu at (155.3, 73.5)
- added R802: DNP_4K7, Resistor_SMD:R_0402_1005Metric, F.Cu at (155.3, 75.5)
- added R803: 1K, Resistor_SMD:R_0402_1005Metric, F.Cu at (155.3, 77.5)
- added R804: 4K7, Resistor_SMD:R_0402_1005Metric, F.Cu at (155.3, 79.5)
- added R805: 1K, Resistor_SMD:R_0402_1005Metric, F.Cu at (155.3, 81.5)
- added R806: 1K, Resistor_SMD:R_0402_1005Metric, F.Cu at (158.2, 69.6)
- added R807: 22R, Resistor_SMD:R_0402_1005Metric, F.Cu at (158.2, 71.6)
- added R808: 22R, Resistor_SMD:R_0402_1005Metric, F.Cu at (158.2, 73.5)
- added R809: 22R, Resistor_SMD:R_0402_1005Metric, F.Cu at (158.2, 75.5)
- added R810: 22R, Resistor_SMD:R_0402_1005Metric, F.Cu at (158.2, 77.5)
- added R811: 22R, Resistor_SMD:R_0402_1005Metric, F.Cu at (158.2, 79.5)
- added R812: 22R, Resistor_SMD:R_0402_1005Metric, F.Cu at (158.2, 81.5)
- added R813: 1K, Resistor_SMD:R_0402_1005Metric, F.Cu at (161.1, 69.6)
- added R814: 1K, Resistor_SMD:R_0402_1005Metric, F.Cu at (161.1, 71.6)
- added R815: 22R, Resistor_SMD:R_0402_1005Metric, F.Cu at (161.1, 73.5)
- added R816: 22R, Resistor_SMD:R_0402_1005Metric, F.Cu at (161.1, 75.5)
- added R817: 22R, Resistor_SMD:R_0402_1005Metric, F.Cu at (161.1, 77.5)
- added R818: 4K7, Resistor_SMD:R_0402_1005Metric, F.Cu at (161.1, 79.5)
- added R819: 4K7, Resistor_SMD:R_0402_1005Metric, F.Cu at (161.1, 81.5)
- added R820: 4K7, Resistor_SMD:R_0402_1005Metric, F.Cu at (164.0, 69.6)
- added R821: 2K49, Resistor_SMD:R_0402_1005Metric, F.Cu at (164.0, 71.6)
- added R822: 510R, Resistor_SMD:R_0402_1005Metric, F.Cu at (164.0, 73.5)
- added R823: 510R, Resistor_SMD:R_0402_1005Metric, F.Cu at (164.0, 75.5)
- added U800: RTL8211F-CG, Package_DFN_QFN:QFN-40-1EP_5x5mm_P0.4mm_EP3.8x3.8mm, F.Cu at (137.9, 95.1)
- added X800: ECS-2520MV-250-BN-TR, Oscillator:Oscillator_SMD_ECS_2520MV-xxx-xx-4Pin_2.5x2.0mm, F.Cu at (143.5, 93.6)
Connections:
- FB1 pad 1: +3V3 -> +3V3_ETH
- FB1 pad 2: Net-(U300-VPHY) -> +3V3

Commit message: finished page 9, USB 2.0 Hub
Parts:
- added C900: 100n, Capacitor_SMD:C_0402_1005Metric, F.Cu at (190.1, 93.7)
- added C901: 100n, Capacitor_SMD:C_0402_1005Metric, F.Cu at (190.1, 95.6)
- added C902: 100n, Capacitor_SMD:C_0402_1005Metric, F.Cu at (190.1, 97.6)
- added C903: 100n, Capacitor_SMD:C_0402_1005Metric, F.Cu at (190.1, 99.6)
- added C904: 100n, Capacitor_SMD:C_0402_1005Metric, F.Cu at (190.1, 101.6)
- added C905: 4u7, Capacitor_SMD:C_0402_1005Metric, F.Cu at (190.1, 103.5)
- added C906: 4u7, Capacitor_SMD:C_0402_1005Metric, F.Cu at (190.1, 105.5)
- added C907: 4u7, Capacitor_SMD:C_0402_1005Metric, F.Cu at (217.0, 108.1)
- added C908: 4u7, Capacitor_SMD:C_0402_1005Metric, F.Cu at (217.0, 110.1)
- added D900: CG0402MLU-3.3G, Diode_SMD:D_0402_1005Metric, F.Cu at (200.8, 105.6)
- added D901: CG0402MLU-3.3G, Diode_SMD:D_0402_1005Metric, F.Cu at (200.8, 107.6)
- added D902: CG0402MLU-3.3G, Diode_SMD:D_0402_1005Metric, F.Cu at (200.8, 109.6)
- added D903: PMEG1030EJ,115, Diode_SMD:D_SOD-323F, F.Cu at (204.4, 110.4)
- added FB900: 120R, Inductor_SMD:L_0402_1005Metric, F.Cu at (205.0, 91.7)
- added J900: GMSB0522132EU, ZeBra_footprints:GMSB0522132EU, F.Cu at (215.4, 98.0)
- added R900: 1K, Resistor_SMD:R_0402_1005Metric, F.Cu at (205.0, 97.7)
- added R901: 22R, Resistor_SMD:R_0402_1005Metric, F.Cu at (205.0, 99.7)
- added R902: 8K06, Resistor_SMD:R_0402_1005Metric, F.Cu at (222.2, 103.5)
- added R903: 12K, Resistor_SMD:R_0402_1005Metric, F.Cu at (205.0, 101.7)
- added R904: 4K7, Resistor_SMD:R_0402_1005Metric, F.Cu at (222.2, 105.5)
- added U900: USB3320C-EZK, ZeBra_footprints:QFN32_5X5MC_MCH, F.Cu at (195.2, 108.4)
- added U901: TPS2051CDBV, Package_TO_SOT_SMD:SOT-23-5, F.Cu at (218.1, 104.9)
- added X900: ECS-2520MV-130-BN-TR, Oscillator:Oscillator_SMD_ECS_2520MV-xxx-xx-4Pin_2.5x2.0mm, F.Cu at (204.1, 106.7)
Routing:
- added copper zone on F.Cu, net +1V8
- removed copper zone on F.Cu, net GND

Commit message: Finished first pass of schematic, needs netclass assignments and double check
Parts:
- added J1000: 10144518-082802LF, ZeBra_footprints:CONN_10144518_AMP, F.Cu at (-15.5, 188.3)
- added J1001: 10144518-082802LF, ZeBra_footprints:CONN_10144518_AMP, F.Cu at (-15.5, 197.6)
- U402: footprint Package_SON:WSON-8-1EP_8x6mm_P1.27mm_EP3.4x4.3mm -> ZeBra_footprints:WSON-8-1EP_8x6mm_P1.27mm_EP3.4x4.3mm
- moved C111 155.1 mm to (-60.3, 172.1)
- moved C115 155.1 mm to (-60.3, 174.1)
- moved C116 155.1 mm to (-60.3, 176.1)
- moved C120 155.1 mm to (-60.3, 178.0)
- moved C121 155.1 mm to (-60.3, 180.0)
- moved C125 155.1 mm to (-57.4, 172.1)
- moved C126 155.1 mm to (-57.4, 174.1)
- moved C128 155.1 mm to (-57.4, 176.1)
- moved C129 155.1 mm to (-57.4, 178.0)
- moved C306 155.1 mm to (48.9, 162.8)
- moved C310 155.1 mm to (48.9, 164.7)
- moved C311 155.1 mm to (48.9, 166.7)
- moved C312 155.1 mm to (48.9, 168.7)
- moved C313 155.1 mm to (48.9, 170.6)
- moved C316 155.1 mm to (51.8, 162.8)
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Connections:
- net /[3] Config, JTAG, Debug/DONE renamed DONE
- U200 pad J16: PL_B35_L24_P -> PL_B35_L24_N
- U200 pad R18: GND -> unconnected-(U200A-IO_L20N_T3_34-PadR18)
- U200 pad R8: (no net) -> GND
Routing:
- net GND: track 0.00 -> 1.13 mm, vias 0 -> 2
- net /[4] Zynq Processing System (PS)/SD_CMD: track 0.00 -> 0.57 mm, vias 0 -> 1
- net +1V35: track 0.00 -> 0.57 mm, vias 0 -> 1
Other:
- board size 255.3 x 107.1 mm -> 90 x 60 mm
- copper layers 2 -> 10
- board text added: "L0 - sig L1 - gnd L2 - pwr L3 - sig L4 - gnd L5 - sig L6 - gnd L7 - sig L8 - gnd L9 - sig"
